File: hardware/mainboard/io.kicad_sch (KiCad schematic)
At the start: 25 parts

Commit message: Design updates
Signed-off-by: gatecat <gatecat@ds0.me>
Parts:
- added D? (x8): PESD3V3L4UF, Package_TO_SOT_SMD:SOT-886, symbol Power_Protection:PESD3V3L4UF
- added J?: DEBUG, symbol Connector_Generic_Shielded:Conn_01x10_Shielded
- added SW?: SW_SPDT, symbol Switch:SW_SPDT
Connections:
- net +1V8PS: now also J?.1 (Pin_1)
- net GND: now also D?.2 (A), D?.2 (A), D?.2 (A), D?.2 (A), D?.2 (A), D?.2 (A), D?.2 (A), D?.2 (A), D?.5 (A), D?.5 (A), D?.5 (A), D?.5 (A), D?.5 (A), D?.5 (A), D?.5 (A), D?.5 (A), J?.10 (Pin_10), J?.SH (Shield), SW?.1 (A)
- new net JTAG_TCK: D?.1 (K1), J?.3 (Pin_3)
- new net JTAG_TDI: D?.1 (K1), J?.2 (Pin_2)
- new net JTAG_TDO: D?.1 (K1), J?.5 (Pin_5)
- new net JTAG_TMS: D?.1 (K1), J?.4 (Pin_4)
- new net POWEROFF: SW?.2 (B)
- new net RECOVERY: D?.1 (K1), J?.9 (Pin_9)
- new net SYS_RESET: D?.1 (K1), J?.8 (Pin_8)
- new net UART_RX: D?.1 (K1), J?.7 (Pin_7)
- new net UART_TX: D?.1 (K1), J?.6 (Pin_6)
- no-connect marks 6 -> 7

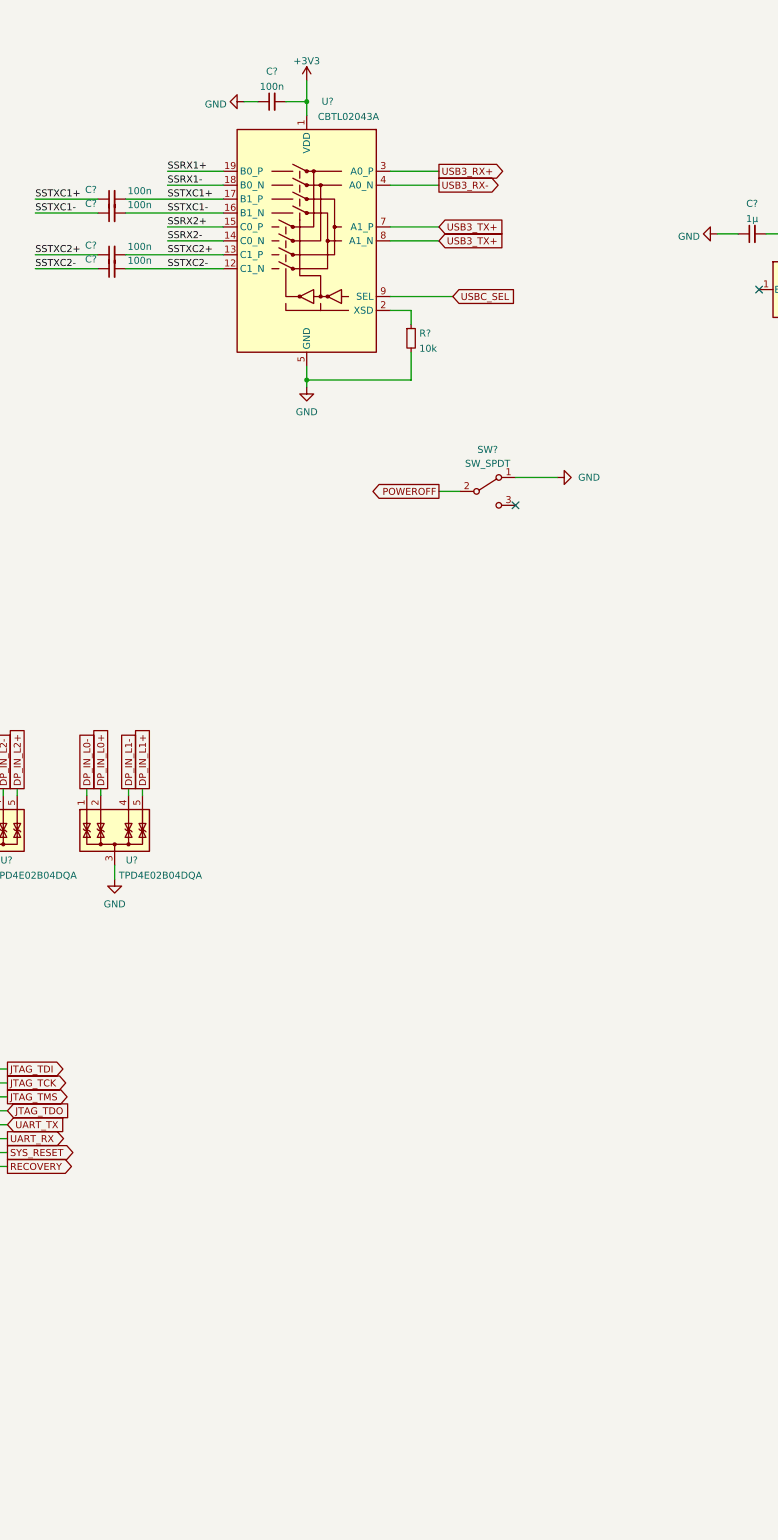
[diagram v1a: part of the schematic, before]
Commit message: Re-add USB-C PD control
Signed-off-by: gatecat <gatecat@ds0.me>
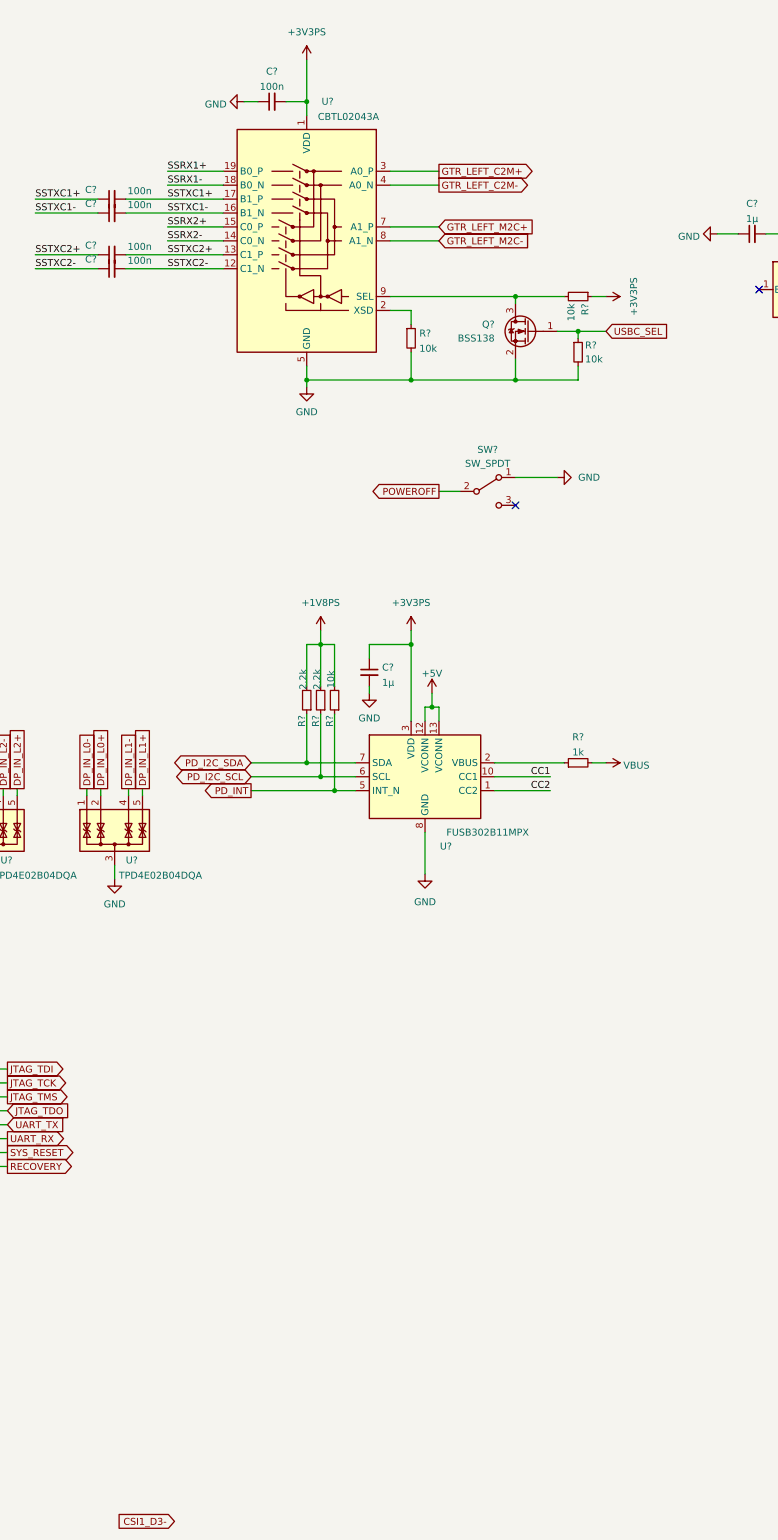
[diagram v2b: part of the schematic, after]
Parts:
- added C?: 1µ, symbol Device:C_Small
- added Q?: BSS138, Package_TO_SOT_SMD:SOT-23, symbol Transistor_FET:BSS138
- added R? (x3): 10k, symbol Device:R_Small
- added R?: 1k, symbol Device:R_Small
- added R? (x2): 2.2k, symbol Device:R_Small
- added U?: FUSB302B11MPX, Package_DFN_QFN:WQFN-14-1EP_2.5x2.5mm_P0.5mm_EP1.45x1.45mm, symbol Interface_USB:FUSB302B11MPX
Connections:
- net +1V8PS: now also R?.2, R?.2, R?.2
- net +3V3: no longer C?.2, U?.1 (VDD), U?.10 (VDD), U?.6 (VDD)
- net +3V3PS: now also C?.2, U?.1 (VDD), U?.10 (VDD), U?.6 (VDD), C?.1, R?.1, U?.3 (VDD), U?.4 (VDD)
- net CC1: now also U?.10 (CC1), U?.11 (CC1)
- net CC2: now also U?.1 (CC2), U?.14 (CC2)
- net GND: now also C?.2, Q?.2 (S), R?.2, U?.15 (GND), U?.8 (GND), U?.9 (GND)
- net USBC_SEL: now also Q?.1 (G), R?.1; no longer U?.9 (SEL)
- net VBUS: now also R?.2
- net USB3_RX+ renamed GTR_LEFT_C2M+
- net USB3_RX- renamed GTR_LEFT_C2M-
- net USB3_TX+ renamed GTR_LEFT_M2C+
- net GTR_LEFT_M2C+: no longer U?.8 (A1_N)
- new net: Q?.3 (D), R?.2, U?.9 (SEL)
- new net: R?.1, U?.2 (VBUS)
- new net +5V: U?.12 (VCONN), U?.13 (VCONN)
- new net GTR_LEFT_M2C-: U?.8 (A1_N)
- new net PD_I2C_SCL: R?.1, U?.6 (SCL)
- new net PD_I2C_SDA: R?.1, U?.7 (SDA)
- new net PD_INT: R?.1, U?.5 (INT_N)

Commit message: ERC fixes
Signed-off-by: gatecat <gatecat@ds0.me>
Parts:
- gave numbers to parts that had none: 44
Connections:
- net +3V3 is gone; now on net +3V3PS: F1.1
- net DP_HPD renamed DP_HPD_3V3

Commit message: Add some footprint mappings
Signed-off-by: gatecat <gatecat@ds0.me>
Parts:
- C54, C55, C56, C57, C58: footprint (none) -> Capacitor_SMD:C_0402_1005Metric
- C59: footprint (none) -> Capacitor_SMD:C_0603_1608Metric
- F1: footprint (none) -> Fuse:Fuse_0805_2012Metric
- J4: footprint (none) -> Connector_USB:USB_C_Receptacle_Amphenol_12401610E4-2A
- R50, R51, R52, R53, R54, R55, R56, R57, R58, R59, R60: footprint (none) -> Resistor_SMD:R_0402_1005Metric
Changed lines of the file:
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@@
     (property "Reference" "C57" (id 0) (at 123.19 71.9414 90))
     (property "Value" "100n" (id 1) (at 132.08 72.1765 90))
-    (property "Footprint" "" (id 2) (at 127 73.66 0)
+    (property "Footprint" "Capacitor_SMD:C_0402_1005Metric" (id 2) (at 127 73.66 0)
       (effects (font (size 1.27 1.27)) hide)
     )
@@
     (property "Reference" "R56" (id 0) (at 166.7469 156.21 90))
     (property "Value" "10k" (id 1) (at 166.982 148.59 90))
-    (property "Footprint" "" (id 2) (at 167.64 152.4 0)
+    (property "Footprint" "Resistor_SMD:R_0402_1005Metric" (id 2) (at 167.64 152.4 0)
       (effects (font (size 1.27 1.27)) hide)
     )
@@
     (property "Reference" "C54" (id 0) (at 123.19 59.2414 90))
     (property "Value" "100n" (id 1) (at 132.08 59.4765 90))
-    (property "Footprint" "" (id 2) (at 127 60.96 0)
+    (property "Footprint" "Capacitor_SMD:C_0402_1005Metric" (id 2) (at 127 60.96 0)
       (effects (font (size 1.27 1.27)) hide)
     )
@@
     (property "Reference" "C56" (id 0) (at 123.19 69.4014 90))
     (property "Value" "100n" (id 1) (at 132.08 69.6365 90))
-    (property "Footprint" "" (id 2) (at 127 71.12 0)
+    (property "Footprint" "Capacitor_SMD:C_0402_1005Metric" (id 2) (at 127 71.12 0)
       (effects (font (size 1.27 1.27)) hide)
     )
@@
     (property "Reference" "R53" (id 0) (at 85.09 48.26 90))
     (property "Value" "5.1k" (id 1) (at 85.09 45.72 90))
-    (property "Footprint" "" (id 2) (at 85.09 43.18 0)
+    (property "Footprint" "Resistor_SMD:R_0402_1005Metric" (id 2) (at 85.09 43.18 0)
       (effects (font (size 1.27 1.27)) hide)
     )
@@
     (property "Reference" "J4" (id 0) (at 49.4665 27.94 0))
     (property "Value" "USB_C_Receptacle" (id 1) (at 49.4665 30.48 0))
-    (property "Footprint" "" (id 2) (at 50.8 60.96 0)
+    (property "Footprint" "Connector_USB:USB_C_Receptacle_Amphenol_12401610E4-2A" (id 2) (at 50.8 60.96 0)
       (effects (font (size 1.27 1.27)) hide)
     )
@@
       (effects (font (size 1.27 1.27)) (justify left))
     )
-    (property "Footprint" "" (id 2) (at 212.09 88.9 0)
+    (property "Footprint" "Resistor_SMD:R_0402_1005Metric" (id 2) (at 212.09 88.9 0)
       (effects (font (size 1.27 1.27)) hide)
     )
@@
     (property "Reference" "R60" (id 0) (at 212.09 159.1269 90))
     (property "Value" "1k" (id 1) (at 212.09 161.902 90))
-    (property "Footprint" "" (id 2) (at 212.09 163.83 0)
+    (property "Footprint" "Resistor_SMD:R_0402_1005Metric" (id 2) (at 212.09 163.83 0)
       (effects (font (size 1.27 1.27)) hide)
     )
@@
     (property "Reference" "R55" (id 0) (at 164.2069 156.21 90))
     (property "Value" "2.2k" (id 1) (at 164.442 148.59 90))
-    (property "Footprint" "" (id 2) (at 165.1 152.4 0)
+    (property "Footprint" "Resistor_SMD:R_0402_1005Metric" (id 2) (at 165.1 152.4 0)
       (effects (font (size 1.27 1.27)) hide)
     )
@@
     (property "Reference" "C58" (id 0) (at 156.21 37.6514 90))
     (property "Value" "100n" (id 1) (at 156.21 40.4265 90))
-    (property "Footprint" "" (id 2) (at 156.21 43.18 0)
+    (property "Footprint" "Capacitor_SMD:C_0402_1005Metric" (id 2) (at 156.21 43.18 0)
       (effects (font (size 1.27 1.27)) hide)
     )
@@
     (property "Reference" "C55" (id 0) (at 123.19 61.7814 90))
     (property "Value" "100n" (id 1) (at 132.08 62.0165 90))
-    (property "Footprint" "" (id 2) (at 127 63.5 0)
+    (property "Footprint" "Capacitor_SMD:C_0402_1005Metric" (id 2) (at 127 63.5 0)
       (effects (font (size 1.27 1.27)) hide)
     )
@@
       (effects (font (size 1.27 1.27)) (justify left))
     )
-    (property "Footprint" "" (id 2) (at 173.99 147.32 0)
+    (property "Footprint" "Capacitor_SMD:C_0603_1608Metric" (id 2) (at 173.99 147.32 0)
       (effects (font (size 1.27 1.27)) hide)
     )
@@
       (effects (font (size 1.27 1.27)) (justify left))
     )
-    (property "Footprint" "" (id 2) (at 212.09 78.74 0)
+    (property "Footprint" "Resistor_SMD:R_0402_1005Metric" (id 2) (at 212.09 78.74 0)
       (effects (font (size 1.27 1.27)) hide)
     )
@@
     (property "Reference" "R52" (id 0) (at 85.09 35.9369 90))
     (property "Value" "5.1k" (id 1) (at 85.09 38.712 90))
-    (property "Footprint" "" (id 2) (at 85.09 40.64 0)
+    (property "Footprint" "Resistor_SMD:R_0402_1005Metric" (id 2) (at 85.09 40.64 0)
       (effects (font (size 1.27 1.27)) hide)
     )
@@
     (property "Reference" "R50" (id 0) (at 80.01 134.9969 90))
     (property "Value" "10k" (id 1) (at 87.63 135.232 90))
-    (property "Footprint" "" (id 2) (at 83.82 135.89 0)
+    (property "Footprint" "Resistor_SMD:R_0402_1005Metric" (id 2) (at 83.82 135.89 0)
       (effects (font (size 1.27 1.27)) hide)
     )
@@
     (property "Reference" "R54" (id 0) (at 161.6669 156.21 90))
     (property "Value" "2.2k" (id 1) (at 161.902 148.59 90))
-    (property "Footprint" "" (id 2) (at 162.56 152.4 0)
+    (property "Footprint" "Resistor_SMD:R_0402_1005Metric" (id 2) (at 162.56 152.4 0)
       (effects (font (size 1.27 1.27)) hide)
     )
@@
     (property "Reference" "R51" (id 0) (at 80.01 140.0769 90))
     (property "Value" "10k" (id 1) (at 87.63 140.312 90))
-    (property "Footprint" "" (id 2) (at 83.82 140.97 0)
+    (property "Footprint" "Resistor_SMD:R_0402_1005Metric" (id 2) (at 83.82 140.97 0)
       (effects (font (size 1.27 1.27)) hide)
     )
@@
     (property "Reference" "F1" (id 0) (at 69.85 175.4845 90))
     (property "Value" "500mA" (id 1) (at 69.85 178.2596 90))
-    (property "Footprint" "" (id 2) (at 64.77 181.61 0)
+    (property "Footprint" "Fuse:Fuse_0805_2012Metric" (id 2) (at 64.77 181.61 0)
       (effects (font (size 1.27 1.27)) (justify left) hide)
     )
@@
       (effects (font (size 1.27 1.27)) (justify left))
     )
-    (property "Footprint" "" (id 2) (at 181.61 86.36 0)
-      (effects (font (size 1.27 1.27)) hide)
-    )
+    (property "Footprint" "Resistor_SMD:R_0402_1005Metric" (id 2) (at 181.61 86.36 0)
+      (effects (font (size 1.27 1.27)) hide)
+    )

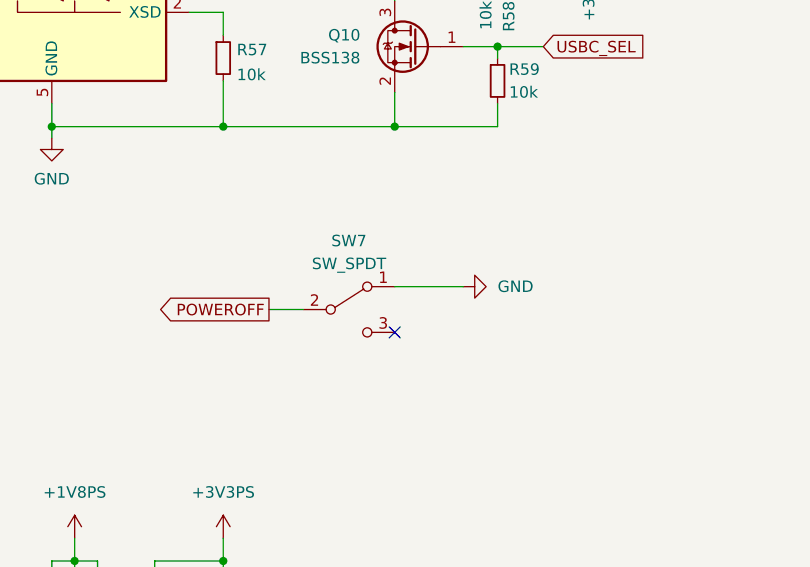
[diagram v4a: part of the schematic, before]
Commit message: Footprint assignments and related fixes
Signed-off-by: gatecat <gatecat@ds0.me>
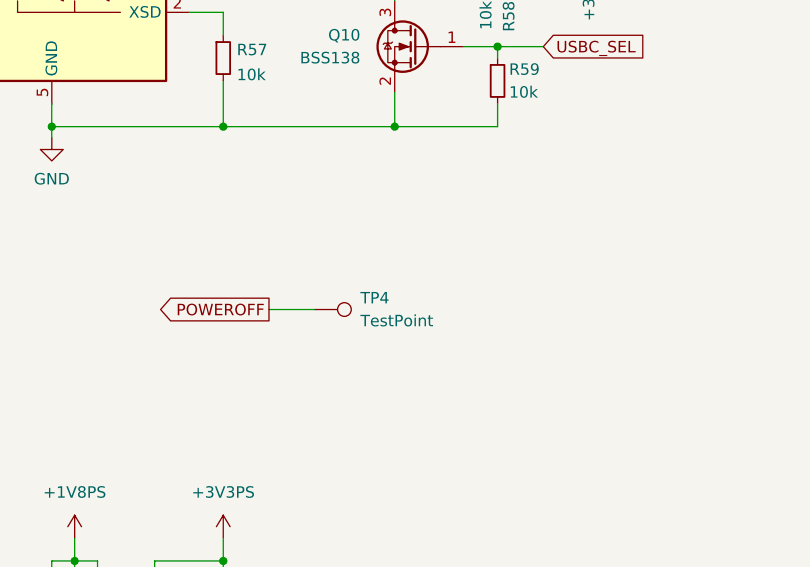
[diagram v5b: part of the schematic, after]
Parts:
- removed SW7: SW_SPDT, symbol Switch:SW_SPDT
- added TP4: TestPoint, TestPoint:TestPoint_Pad_D2.0mm, symbol Connector:TestPoint
- C61: footprint Capacitor_SMD:C_0805_2012Metric_Pad1.15x1.40mm_HandSolder -> Capacitor_SMD:C_0805_2012Metric
- J3: footprint (none) -> meowality:HARTING_10B1_JACK_AH
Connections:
- net POWEROFF: now also TP4.1
- no-connect marks 7 -> 6
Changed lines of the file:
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@@
   (no_connect (at 62.23 93.98))
   (no_connect (at 299.72 69.85))
-  (no_connect (at 200.66 116.84))
   (no_connect (at 245.11 77.47))
   (no_connect (at 299.72 80.01))
@@
     (stroke (width 0) (type default) (color 0 0 0 0))
   )
+  (wire (pts (xy 186.69 114.3) (xy 191.77 114.3))
+    (stroke (width 0) (type default) (color 0 0 0 0))
+  )
   (wire (pts (xy 63.5 250.19) (xy 63.5 260.35))
     (stroke (width 0) (type default) (color 0 0 0 0))
@@
     (stroke (width 0) (type default) (color 0 0 0 0))
   )
-  (wire (pts (xy 186.69 114.3) (xy 190.5 114.3))
-    (stroke (width 0) (type default) (color 0 0 0 0))
-  )
   (wire (pts (xy 99.568 168.5485) (xy 99.568 169.8185))
     (stroke (width 0) (type default) (color 0 0 0 0))
@@
   )
   (wire (pts (xy 72.39 180.34) (xy 77.47 180.34))
-    (stroke (width 0) (type default) (color 0 0 0 0))
-  )
-  (wire (pts (xy 200.66 111.76) (xy 208.28 111.76))
     (stroke (width 0) (type default) (color 0 0 0 0))
   )
@@
     (pin "4")
   )
-  (symbol (lib_id "power:GND") (at 208.28 111.76 90) (unit 1)
-    (in_bom yes) (on_board yes) (fields_autoplaced)
-    (property "Reference" "#PWR0334" (id 0) (at 214.63 111.76 0)
-      (effects (font (size 1.27 1.27)) hide)
-    )
-    (property "Value" "GND" (id 1) (at 212.09 111.7599 90)
-      (effects (font (size 1.27 1.27)) (justify right))
-    )
-    (property "Footprint" "" (id 2) (at 208.28 111.76 0)
-      (effects (font (size 1.27 1.27)) hide)
-    )
-    (property "Datasheet" "" (id 3) (at 208.28 111.76 0)
-      (effects (font (size 1.27 1.27)) hide)
-    )
-    (pin "1")
-  )
   (symbol (lib_id "power:GND") (at 184.15 184.15 0) (unit 1)
     (in_bom yes) (on_board yes) (fields_autoplaced)
@@
     (pin "1")
   )
+  (symbol (lib_id "Connector:TestPoint") (at 191.77 114.3 270) (unit 1)
+    (in_bom yes) (on_board yes) (fields_autoplaced)
+    (property "Reference" "TP4" (id 0) (at 196.85 113.0299 90)
+      (effects (font (size 1.27 1.27)) (justify left))
+    )
+    (property "Value" "TestPoint" (id 1) (at 196.85 115.5699 90)
+      (effects (font (size 1.27 1.27)) (justify left))
+    )
+    (property "Footprint" "TestPoint:TestPoint_Pad_D2.0mm" (id 2) (at 191.77 119.38 0)
+      (effects (font (size 1.27 1.27)) hide)
+    )
+    (property "Datasheet" "~" (id 3) (at 191.77 119.38 0)
+      (effects (font (size 1.27 1.27)) hide)
+    )
+    (pin "1")
+  )
   (symbol (lib_id "power:GND") (at 127.508 185.0585 0) (unit 1)
     (in_bom yes) (on_board yes) (fields_autoplaced)
@@
     (pin "2")
     (pin "5")
-  )
-  (symbol (lib_id "Switch:SW_SPDT") (at 195.58 114.3 0) (unit 1)
-    (in_bom yes) (on_board yes) (fields_autoplaced)
-    (property "Reference" "SW7" (id 0) (at 195.58 106.68 0))
-    (property "Value" "SW_SPDT" (id 1) (at 195.58 109.22 0))
-    (property "Footprint" "" (id 2) (at 195.58 114.3 0)
-      (effects (font (size 1.27 1.27)) hide)
-    )
-    (property "Datasheet" "~" (id 3) (at 195.58 114.3 0)
-      (effects (font (size 1.27 1.27)) hide)
-    )
-    (pin "1")
-    (pin "2")
-    (pin "3")
   )
   (symbol (lib_id "power:GND") (at 44.45 262.89 0) (unit 1)
@@
       (effects (font (size 1.27 1.27)) (justify left))
     )
-    (property "Footprint" "Capacitor_SMD:C_0805_2012Metric_Pad1.15x1.40mm_HandSolder" (id 2) (at 266.7 52.07 0)
+    (property "Footprint" "Capacitor_SMD:C_0805_2012Metric" (id 2) (at 266.7 52.07 0)
       (effects (font (size 1.27 1.27)) hide)
     )
@@
     (property "Reference" "J3" (id 0) (at 44.45 210.82 0))
     (property "Value" "DEBUG" (id 1) (at 44.45 213.36 0))
-    (property "Footprint" "" (id 2) (at 44.45 227.33 0)
-      (effects (font (size 1.27 1.27)) hide)
-    )
+    (property "Footprint" "meowality:HARTING_10B1_JACK_AH" (id 2) (at 44.45 227.33 0)
+      (effects (font (size 1.27 1.27)) hide)
+    )
